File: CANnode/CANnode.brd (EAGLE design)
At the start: 59.8 x 58.3 mm, 245 parts, among them IC1 ISO1050DUB, IC2 ISO1050DUB, Q1 FDV302P, Q3 FDV302P, U1 LM324PW, U10 FT2232HL, U11 93LC56C-I/SN, U2 TPS70445_PWP_24, U3 LM324PW, U4 LM324PW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

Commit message: Layout changes.
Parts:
- added C76: .1uF, rcl:C0402
- added D36: (no value), zetex:SOD323
- C7: value (none) -> .1uF
- R3: value 499k -> 250
- moved TP1 30.3 mm to (56.4, 49.1)
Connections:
- net +3V3: now also C76.1
- net GND: now also C76.2
- net JTAG_SEL: now also Q3.3
- net N$12: now also D36.1
- net N$13: now also D36.2
- net SCI1_RX: now also U7.94
- net SCI1_TX: now also U7.95
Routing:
- net CGND: track 108.1 -> 160.4 mm
- net N$12: track 4.85 -> 50.1 mm, vias 0 -> 2
- net SCI1_TX: track 0.00 -> 10.1 mm, vias 0 -> 1
- net SCI1_RX: track 0.00 -> 6.49 mm, vias 0 -> 1
- net +5V: track 41.1 -> 37.3 mm, vias 13 -> 14
- net GND: track 85.7 -> 82.8 mm
- net N$13: track 0.00 -> 1.45 mm
- net +3V3: track 81.6 -> 82.1 mm, vias 58 -> 57
- net +1V8: vias 12 -> 11

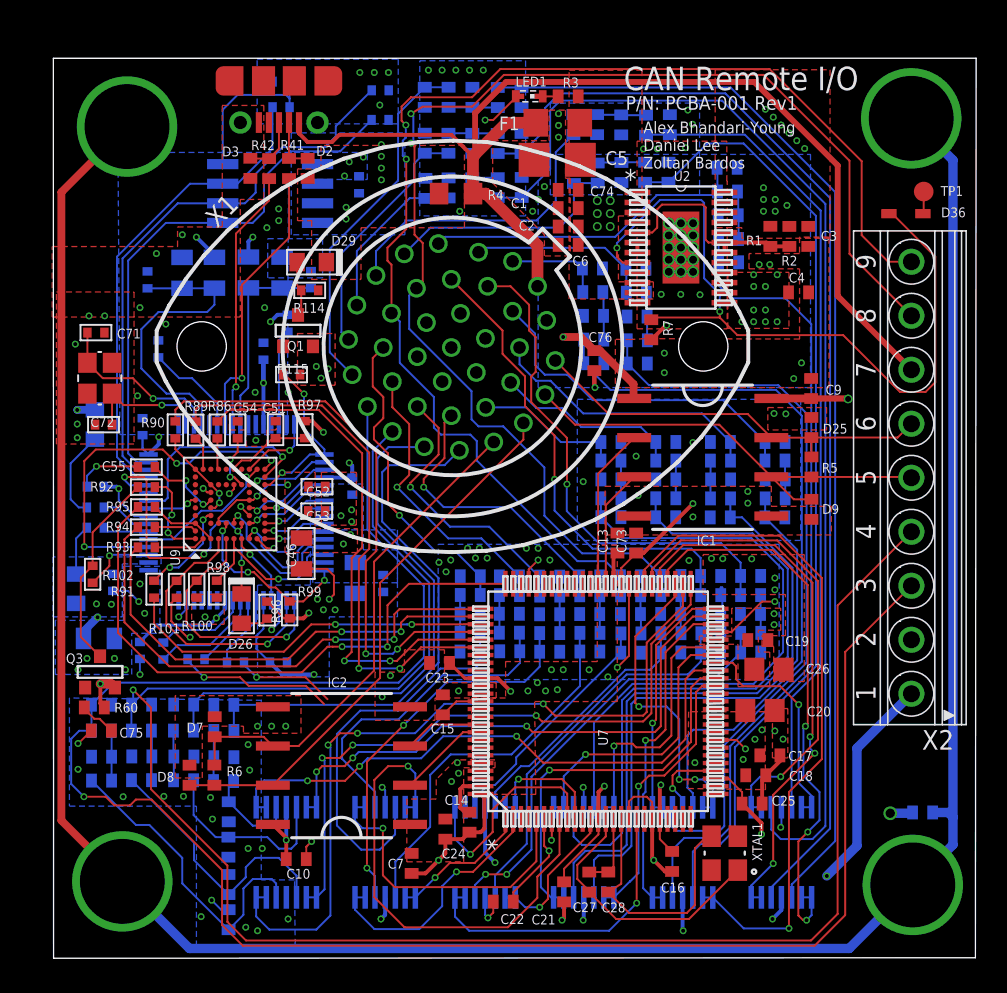
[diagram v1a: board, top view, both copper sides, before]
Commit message: Modified 5V pour for CAN
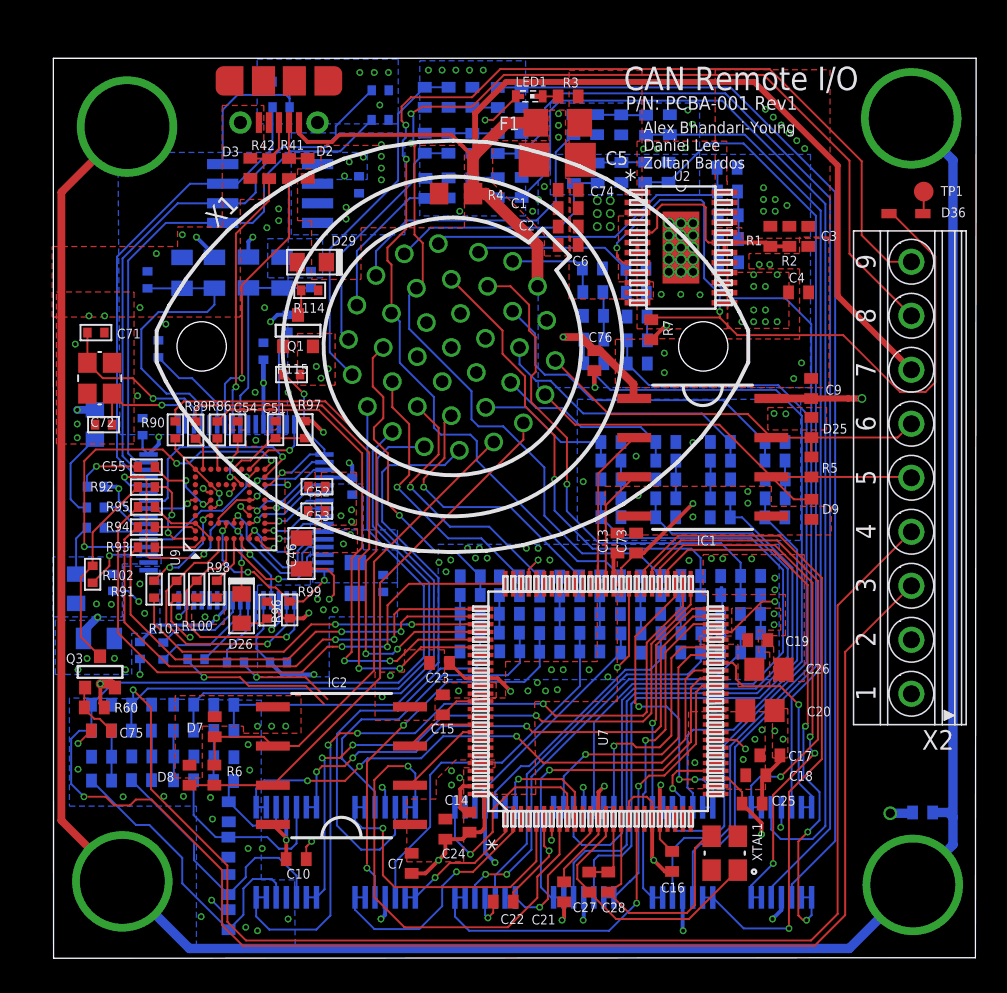
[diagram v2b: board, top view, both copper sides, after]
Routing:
- net +5V: track 37.3 -> 24.1 mm, vias 14 -> 13
- net JTAG_SEL: track 2.51 -> 3.85 mm
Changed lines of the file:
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@@
 <setting verticaltext="up"/>
 </settings>
-<grid distance="1" unitdist="mil" unit="mil" style="lines" multiple="1" display="no" altdistance="10" altunitdist="mil" altunit="mil"/>
+<grid distance="3" unitdist="mil" unit="mil" style="lines" multiple="1" display="no" altdistance="10" altunitdist="mil" altunit="mil"/>
 <layers>
 <layer number="1" name="Top" color="12" fill="1" visible="yes" active="yes"/>
@@
 <layer number="27" name="tValues" color="7" fill="1" visible="no" active="yes"/>
 <layer number="28" name="bValues" color="7" fill="1" visible="no" active="yes"/>
-<layer number="29" name="tStop" color="7" fill="3" visible="no" active="yes"/>
+<layer number="29" name="tStop" color="7" fill="3" visible="yes" active="yes"/>
 <layer number="30" name="bStop" color="7" fill="6" visible="no" active="yes"/>
 <layer number="31" name="tCream" color="7" fill="4" visible="no" active="yes"/>
@@
 <vertex x="28.61261875" y="11.71345"/>
 </polygon>
-<via x="26.25041875" y="11.35785" extent="1-16" drill="0.254"/>
-<via x="25.79321875" y="10.82445" extent="1-16" drill="0.254"/>
-<via x="26.17421875" y="12.04365" extent="1-16" drill="0.254"/>
+<via x="26.32661875" y="11.05305" extent="1-16" drill="0.254"/>
+<via x="25.79321875" y="10.59585" extent="1-16" drill="0.254"/>
+<via x="25.79321875" y="11.51025" extent="1-16" drill="0.254"/>
 <wire x1="27.674025" y1="17.516084375" x2="28.778984375" y2="17.516084375" width="0.254" layer="1"/>
 <wire x1="28.778984375" y1="17.516084375" x2="29.62861875" y2="16.66645" width="0.254" layer="1"/>
@@
 <wire x1="34.11974375" y1="19.23359375" x2="34.107053125" y2="19.246284375" width="0.127" layer="16"/>
 <wire x1="34.11974375" y1="19.23359375" x2="34.11974375" y2="17.017375" width="0.127" layer="16"/>
-<wire x1="34.11974375" y1="17.017375" x2="29.67941875" y2="12.57705" width="0.127" layer="16"/>
-<wire x1="29.67941875" y1="12.57705" x2="25.74050625" y2="12.57705" width="0.127" layer="16"/>
-<wire x1="25.74050625" y1="12.57705" x2="24.407015625" y2="11.243559375" width="0.127" layer="16"/>
+<wire x1="34.11974375" y1="17.017375" x2="29.06981875" y2="12.04365" width="0.127" layer="16"/>
+<wire x1="29.06981875" y1="12.04365" x2="25.13090625" y2="12.04365" width="0.127" layer="16"/>
+<wire x1="25.13090625" y1="12.04365" x2="24.407015625" y2="11.243559375" width="0.127" layer="16"/>
 <wire x1="24.407015625" y1="11.243559375" x2="24.407015625" y2="7.87423125" width="0.127" layer="16"/>
 <wire x1="22.15364375" y1="5.620859375" x2="24.407015625" y2="7.87423125" width="0.127" layer="16"/>
@@
 <contactref element="R52" pad="2"/>
 <contactref element="R51" pad="1"/>
-<wire x1="27.309546875" y1="9.1472875" x2="27.309546875" y2="9.749978125" width="0.127" layer="16"/>
-<wire x1="27.309546875" y1="9.749978125" x2="28.15541875" y2="10.59585" width="0.127" layer="16"/>
-<wire x1="28.15541875" y1="10.59585" x2="28.61261875" y2="10.59585" width="0.127" layer="16"/>
-<wire x1="28.61261875" y1="10.59585" x2="29.98421875" y2="11.96745" width="0.127" layer="16"/>
-<wire x1="36.76679375" y1="19.16974375" x2="29.98421875" y2="12.38716875" width="0.127" layer="16"/>
-<wire x1="29.98421875" y1="12.38716875" x2="29.98421875" y2="11.96745" width="0.127" layer="16"/>
+<wire x1="36.76679375" y1="19.16974375" x2="27.309546875" y2="9.712496875" width="0.127" layer="16"/>
 <wire x1="36.76989375" y1="20.420815625" x2="36.76679375" y2="20.420815625" width="0.127" layer="16"/>
 <wire x1="36.76679375" y1="20.420815625" x2="36.76679375" y2="19.16974375" width="0.127" layer="16"/>
+<wire x1="27.309546875" y1="9.712496875" x2="27.309546875" y2="9.1472875" width="0.127" layer="16"/>
 </signal>
 <signal name="D5_3V3">
@@
 </polygon>
 <polygon width="0.127" layer="15">
-<vertex x="38.67101875" y="49.45785"/>
+<vertex x="37.14701875" y="49.45785"/>
 <vertex x="21.57681875" y="49.45785"/>
 <vertex x="21.57681875" y="11.12925"/>
@@
 <vertex x="25.36141875" y="5.92225"/>
 <vertex x="25.36141875" y="42.67605"/>
-<vertex x="38.67101875" y="42.67605"/>
+<vertex x="37.14701875" y="42.67605"/>
 </polygon>
 <via x="35.24201875" y="46.79085" extent="1-16" drill="0.381"/>
@@
 <via x="46.59581875" y="1.90905" extent="1-16" drill="0.254"/>
 <contactref element="X2" pad="1"/>
-<via x="50.1142" y="4.699" extent="1-16" drill="0.254"/>
-<via x="51.49801875" y="35.61485" extent="1-16" drill="0.381"/>
+<via x="52.39078125" y="35.647675" extent="1-16" drill="0.381"/>
 <wire x1="46.52205625" y1="35.64653125" x2="51.49801875" y2="35.64653125" width="0.4064" layer="1"/>
-<wire x1="51.49801875" y1="35.64653125" x2="51.49801875" y2="35.61485" width="0.4064" layer="1"/>
-<wire x1="55.599" y1="16.5075" x2="52.07" y2="12.9785" width="0.6096" layer="16"/>
-<wire x1="52.07" y1="12.9785" x2="52.07" y2="6.6548" width="0.6096" layer="16"/>
-<wire x1="52.07" y1="6.6548" x2="50.1142" y2="4.699" width="0.6096" layer="16"/>
-<wire x1="37.84276875" y1="42.50255625" x2="46.52205625" y2="35.64653125" width="0" layer="19" extent="1-1"/>
+<wire x1="51.49801875" y1="35.64653125" x2="52.39078125" y2="35.647675" width="0.4064" layer="1"/>
+<polygon width="0.254" layer="15" rank="2">
+<vertex x="59.3598" y="-0.1524"/>
+<vertex x="48.6156" y="-0.1524"/>
+<vertex x="48.6156" y="8.3058"/>
+<vertex x="52.0446" y="8.3058"/>
+<vertex x="52.0446" y="37.2618"/>
+<vertex x="59.3598" y="37.2618"/>
+</polygon>
 </signal>
 <signal name="N$45">
@@
 <wire x1="2.9868" y1="14.8844" x2="3.7488" y2="14.1224" width="0.127" layer="1"/>
 <contactref element="Q3" pad="3"/>
-<wire x1="2.046590625" y1="16.90850625" x2="2.046590625" y2="15.675990625" width="0" layer="19" extent="1-1"/>
+<wire x1="2.046590625" y1="16.90850625" x2="1.9916" y2="16.90850625" width="0.127" layer="1"/>
+<wire x1="1.9916" y1="16.90850625" x2="1.9916" y2="15.621" width="0.127" layer="1"/>
 </signal>
 <signal name="DM">
@@
 <wire x1="13.1572" y1="17.5768" x2="16.3322" y2="17.5768" width="0.127" layer="1"/>
 <wire x1="16.3322" y1="17.5768" x2="17.7546" y2="16.1544" width="0.127" layer="1"/>
-<wire x1="17.7546" y1="16.1544" x2="27.674025" y2="13.01609375" width="0" layer="19" extent="1-16"/>
+<wire x1="17.7546" y1="16.1544" x2="27.674025" y2="13.01609375" width="0" layer="19" extent="1-1"/>
 </signal>
 <signal name="SCI1_TX">
@@
 <wire x1="12.6492" y1="17.018" x2="16.3576" y2="17.018" width="0.127" layer="1"/>
 <wire x1="16.3576" y1="17.018" x2="17.526" y2="15.8496" width="0.127" layer="1"/>
-<wire x1="17.526" y1="15.8496" x2="27.674025" y2="12.51609375" width="0" layer="19" extent="1-16"/>
+<wire x1="17.526" y1="15.8496" x2="27.674025" y2="12.51609375" width="0" layer="19" extent="1-1"/>
 </signal>
 <signal name="N$38">

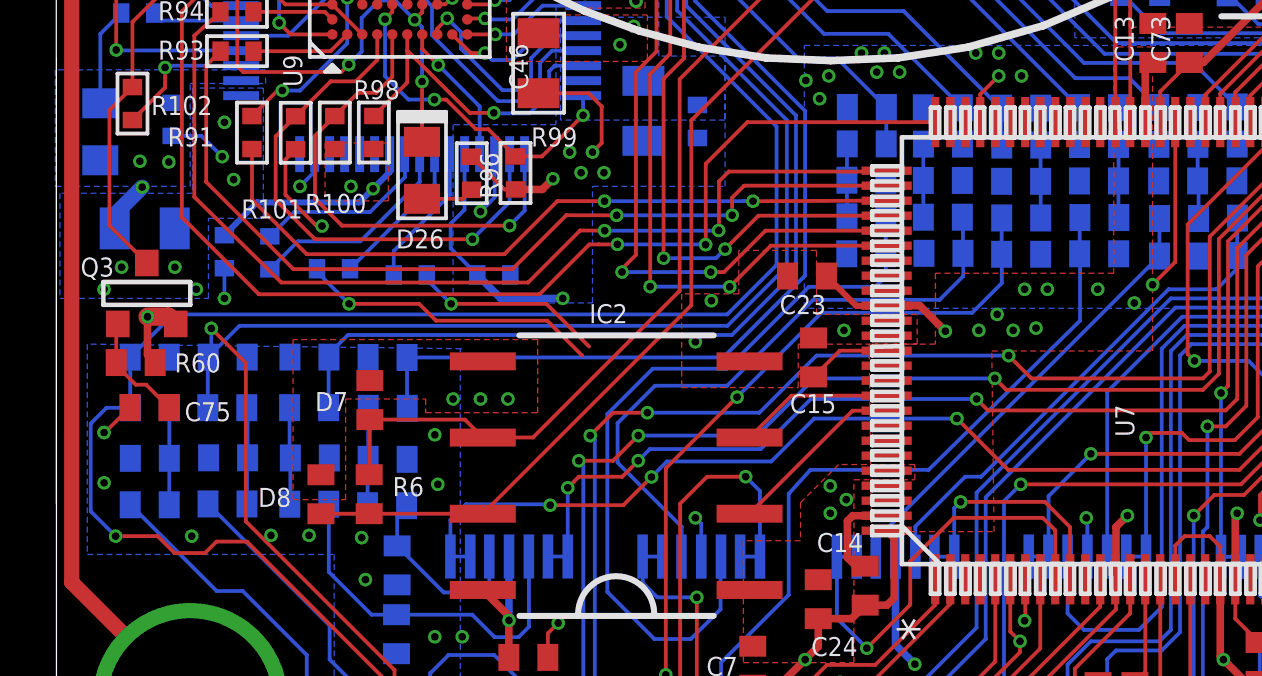
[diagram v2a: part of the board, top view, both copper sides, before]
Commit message: Routed SCI1_TX & RX
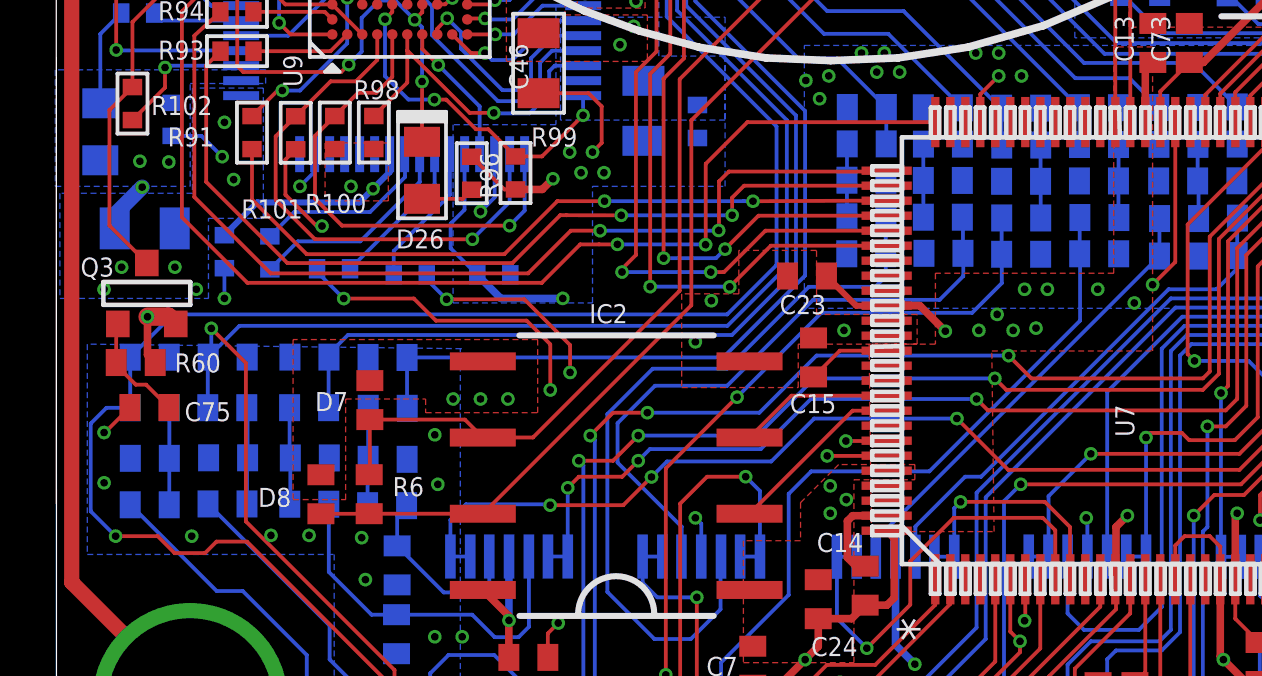
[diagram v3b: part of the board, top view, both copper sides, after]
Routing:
- net SCI1_TX: track 10.1 -> 22.5 mm, vias 1 -> 3
- net SCI1_RX: track 6.49 -> 18.3 mm, vias 1 -> 3

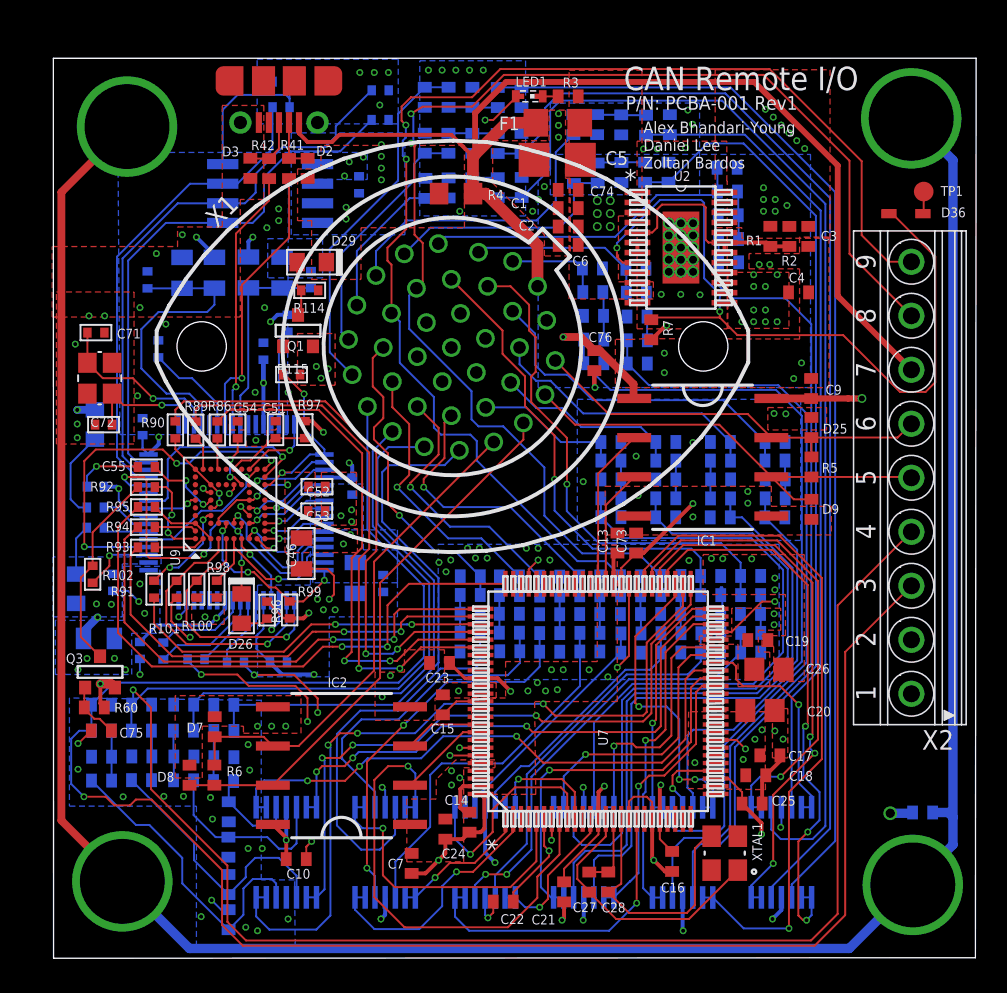
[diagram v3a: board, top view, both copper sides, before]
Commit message: Worked on DRC errors. Solved Polygon errors and overlapping erors. Reduced via sizes for some connections.
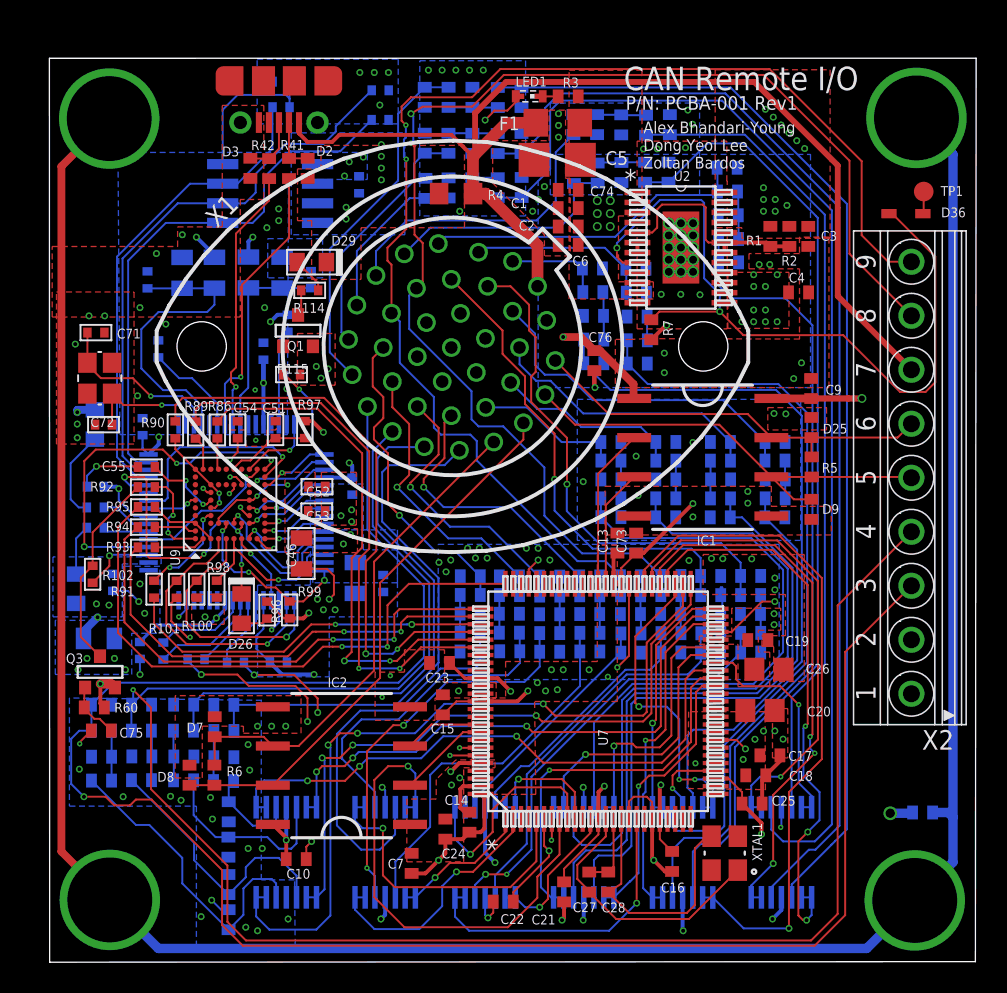
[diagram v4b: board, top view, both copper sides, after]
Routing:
- net +1V2: track 13.8 -> 17.1 mm
- net +3V3: track 82.1 -> 84.4 mm
- net CGND: track 160.4 -> 162.2 mm
- net +1V8: track 20.3 -> 19.3 mm
- net N$37: track 1.49 -> 2.39 mm
- net A5_3V3: track 73.7 -> 74.5 mm
- net A6_3V3: track 74.7 -> 75.4 mm
- net A4_3V3: track 71.6 -> 72.2 mm
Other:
- board size 59.8 x 58.3 mm -> 60.1 x 58.6 mm
- board text added: "Alex Bhandari-Young Dong Yeol Lee Zoltan Bardos"
- board text removed: "Alex Bhandari-Young Daniel Lee Zoltan Bardos"

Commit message: Post Bei review. USB runs closer together. CAN and JTAG need to be rerouted a bit.
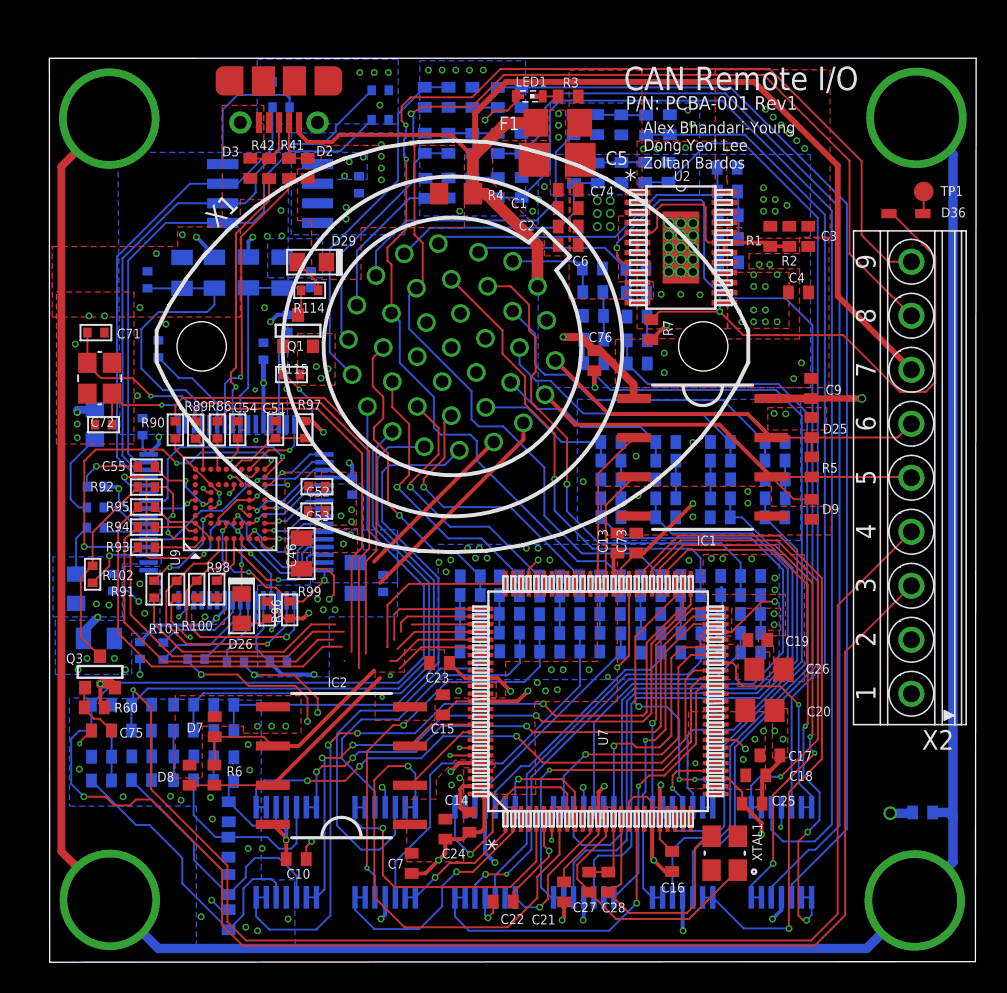
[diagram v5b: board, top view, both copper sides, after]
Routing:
- net CAN2L: track 32.5 -> 25.5 mm
- net CAN2H: track 35.6 -> 29.5 mm
- net MCU_TDO: track 24.3 -> 19.4 mm, vias 2 -> 0
- net MCU_TRSTN: track 33.1 -> 29.1 mm, vias 2 -> 0
- net MCU_RTCK: track 34.3 -> 30.5 mm, vias 2 -> 0
- net MCU_TDI: track 29.9 -> 26.2 mm, vias 2 -> 0
- net MCU_TMS: track 38.5 -> 35.6 mm, vias 2 -> 0
- net MCU_RESET: track 36.3 -> 33.7 mm, vias 2 -> 0
- net MCU_TCK: track 37.2 -> 35.0 mm, vias 2 -> 0
